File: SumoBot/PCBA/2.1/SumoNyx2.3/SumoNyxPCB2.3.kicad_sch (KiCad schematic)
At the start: 16 parts, among them J1 Conn_01x06_Male, J2 BATT 7V5, J3 MOTOR, J4 BACK 7 LED, Q1 AO3422, U1 AZ1117IH-5.0TRG1, U2 NRF24L01_Breakout, U3 DRV8833BRKT

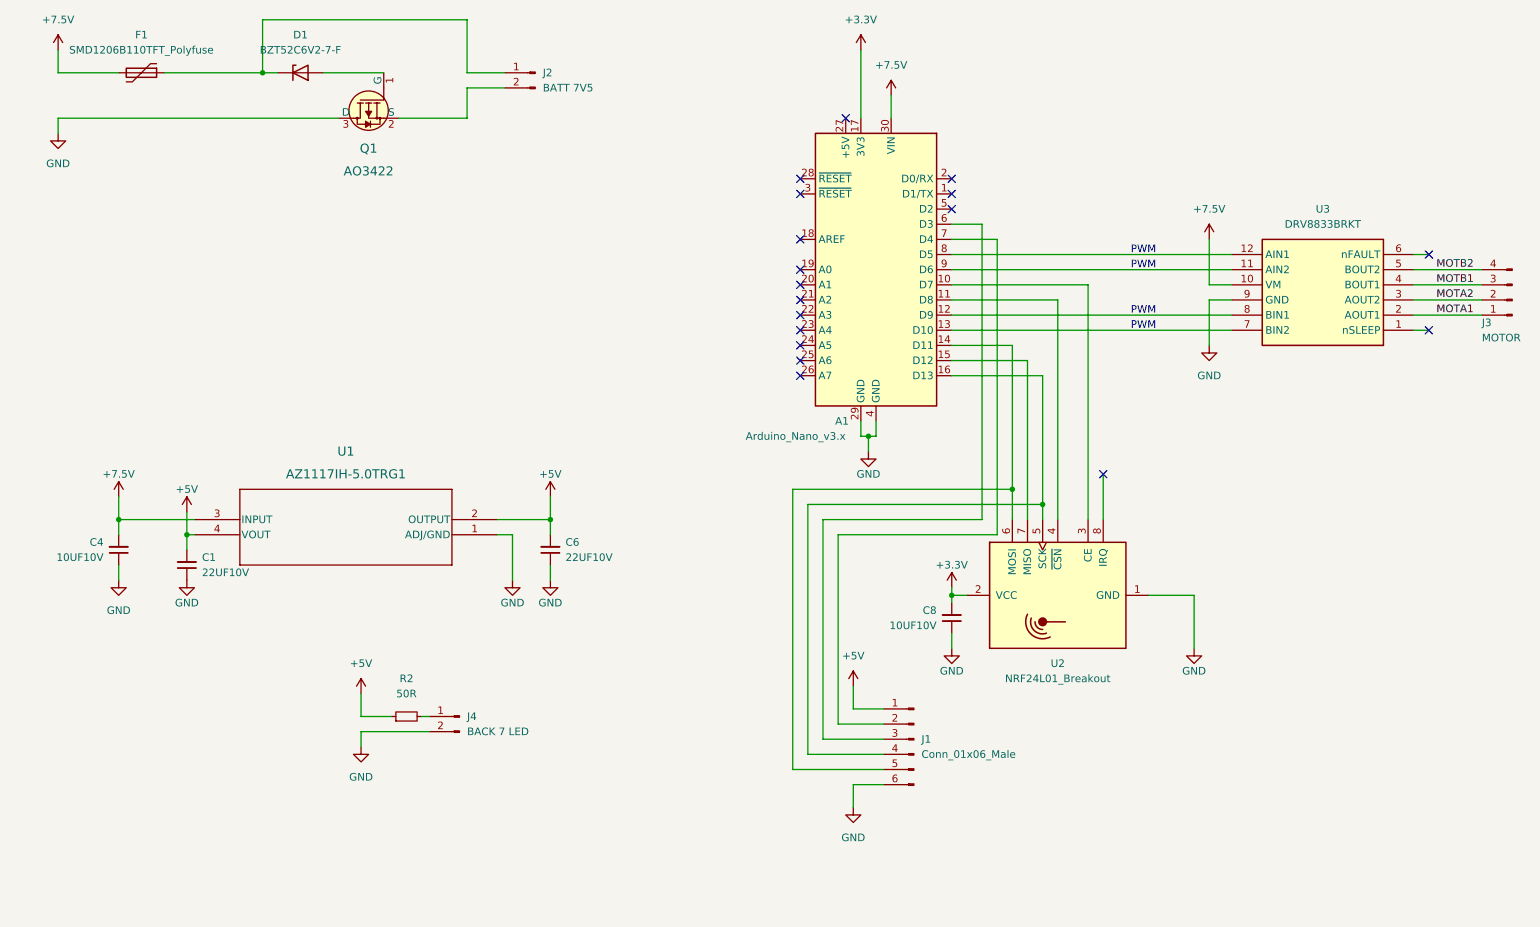
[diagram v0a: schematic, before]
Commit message: added notes to sumonyx pcbs
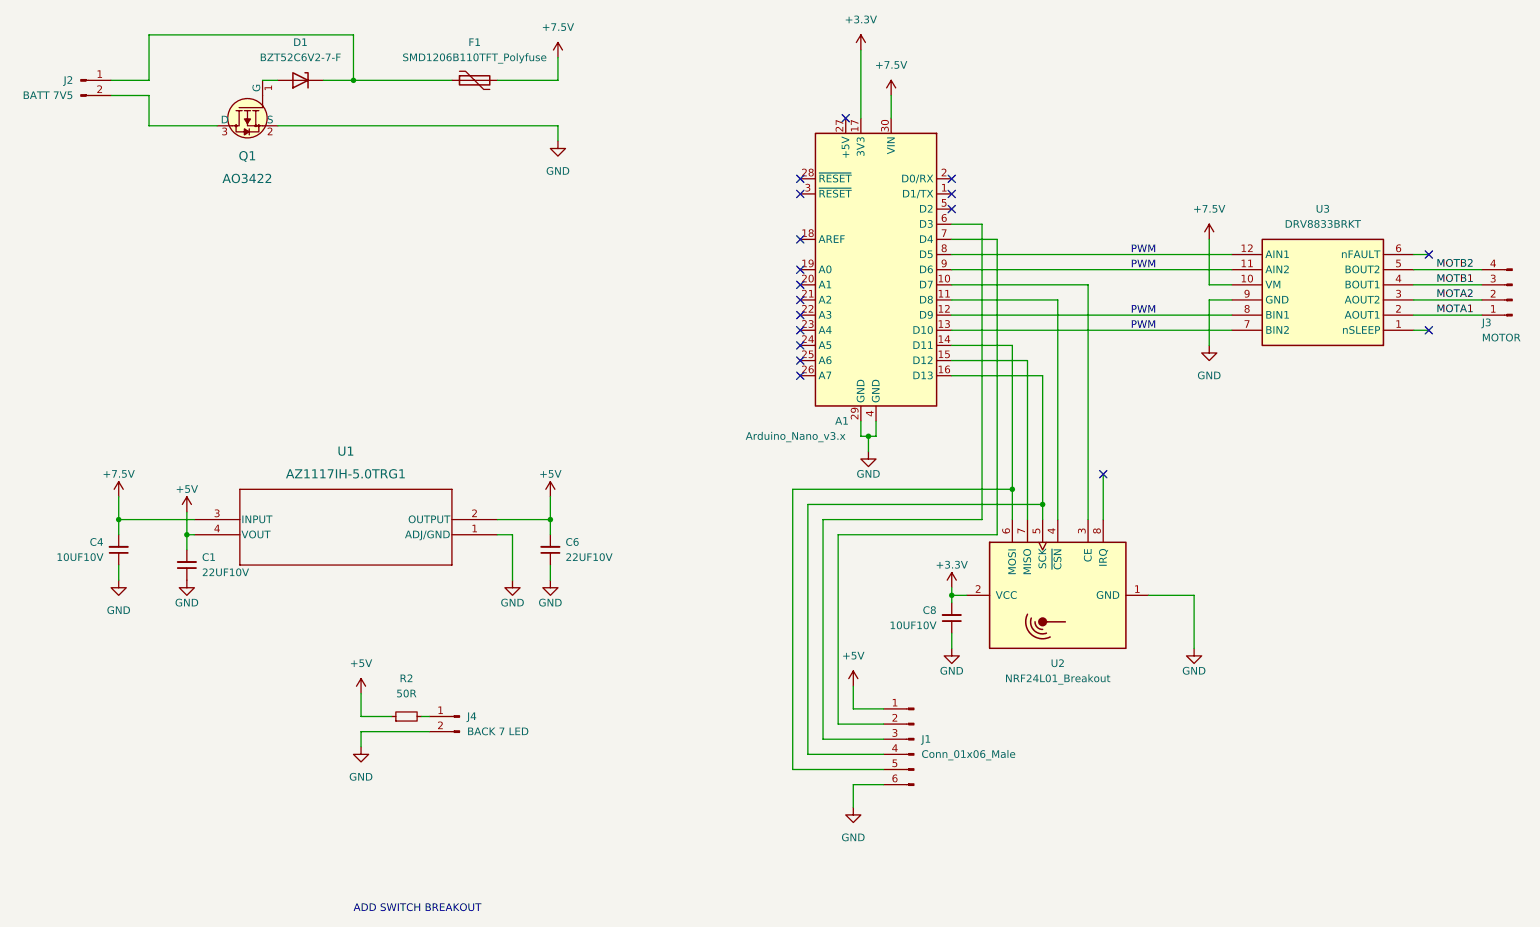
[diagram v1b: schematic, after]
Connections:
- net GND: now also Q1.2 (S); no longer Q1.3 (D)
- net at J2.2 (Pin_2): now also Q1.3 (D); no longer Q1.2 (S)
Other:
- note added: "ADD SWITCH BREAKOUT"
- moved on the sheet: D1, F1, J2, Q1

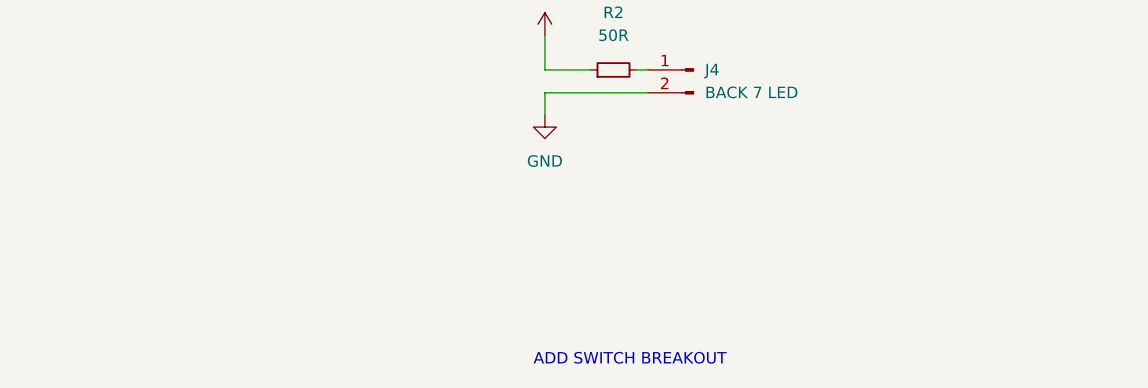
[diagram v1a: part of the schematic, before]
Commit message: sumonyx pcb change to visor ic
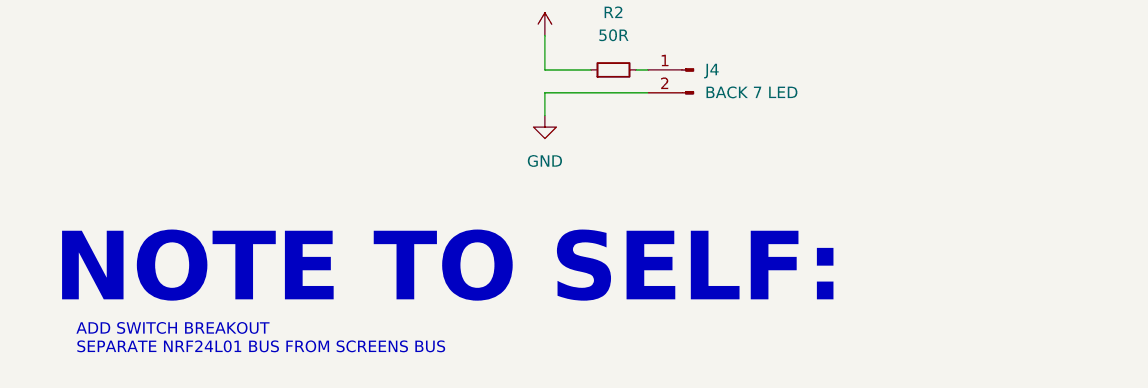
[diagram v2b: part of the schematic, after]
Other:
- note added: "ADD SWITCH BREAKOUT SEPARATE NRF24L01 BUS FROM SCREENS BUS"
- note added: "NOTE TO SELF:"
- note removed: "ADD SWITCH BREAKOUT"
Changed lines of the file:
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@@
     (stroke (width 0) (type default))
   )
-  (text "ADD SWITCH BREAKOUT" (at 68.58 167.64 0)
+  (text "NOTE TO SELF:" (at 15.24 161.29 0)
+    (effects (font (size 7.62 7.62) (thickness 1.524) bold) (justify left bottom))
+  )
+  (text "ADD SWITCH BREAKOUT\nSEPARATE NRF24L01 BUS FROM SCREENS BUS"
+    (at 17.78 166.37 0)
     (effects (font (size 1.27 1.27)) (justify left bottom))
   )

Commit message: main 3.1 edit actualy done now i think...
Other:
- moved on the sheet: D1, F1, Q1
